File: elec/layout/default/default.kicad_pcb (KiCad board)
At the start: 4 copper layers, 76 x 144 mm, 118 parts, among them J1 ?, J2 ?, Q1 ?, Q2 ?, SW1 ?, SW10 ?, SW11 ?, SW12 ?, SW13 ?, SW14 ?, SW15 ?, SW16 ?, SW17 ?, SW18 ?, SW19 ?, SW2 ?, SW20 ?, SW21 ?, SW22 ?, SW23 ?, SW24 ?, SW25 ?, SW26 ?, SW27 ?, SW28 ?, SW29 ?, SW3 ?, SW30 ?, SW31 ?, SW32 ?, SW33 ?, SW34 ?, SW35 ?, SW36 ?, SW37 ?, SW38 ?, SW39 ?, SW4 ?, SW40 ?, SW5 ?, SW6 ?, SW7 ?, SW8 ?, SW9 ?, U1 ?, U2 ?, U3 ?, U4 ?, U5 ?, U6 ?

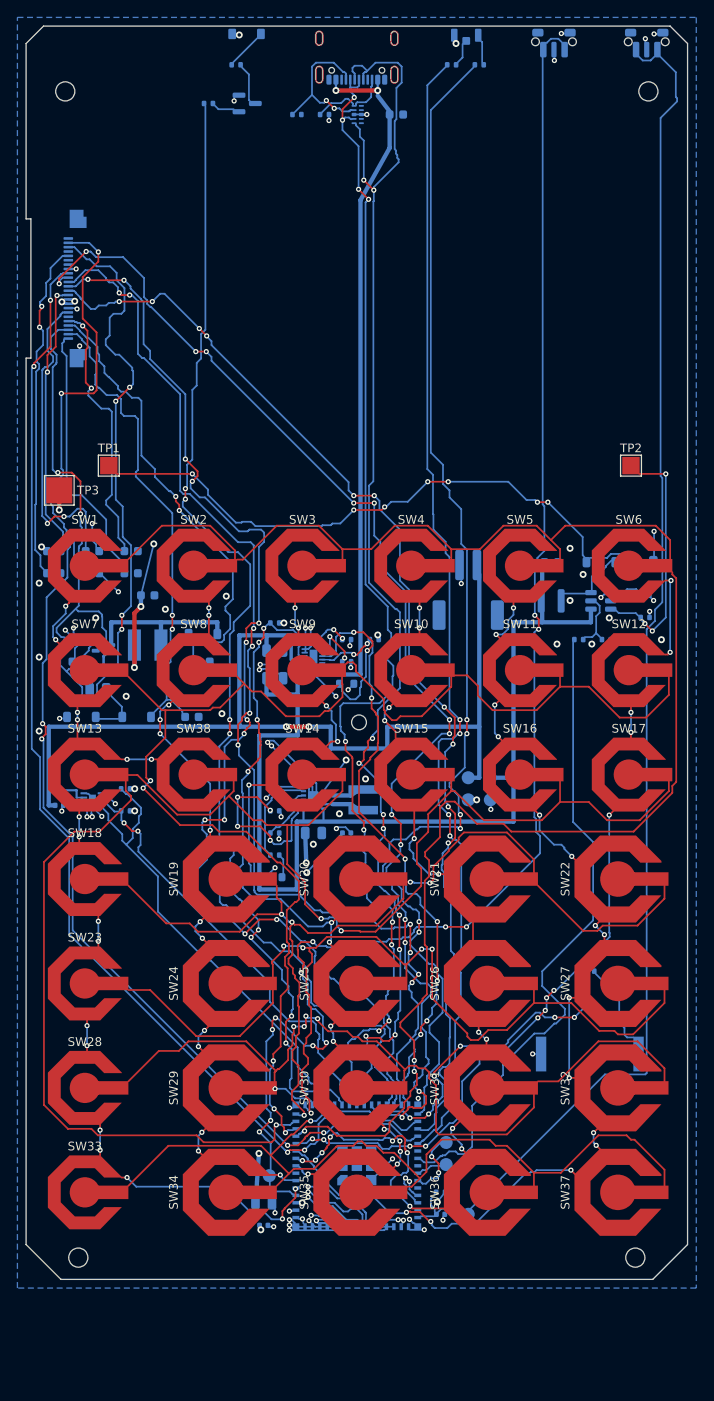
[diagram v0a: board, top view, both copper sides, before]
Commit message: mip: LS032 circuit, 155 mm board, six-LED sliver
display.ato: the e-paper booster is replaced by a TPS610997 5 V boost
(VDD and VDDA together, as Sharp allows), J2 is the Hirose FH34SRJ-10S with
panel pin n on connector pin n, and an RV-8263-C7 on the I2C bus supplies
EXTCOMIN from CLKOUT, gated by CLKOE on IO36. Footprints for the three from
the Hirose catalogue, TI YFF0006 drawing and Micro Crystal datasheet.

Board: variant.py DROP = 11, BOARD_H = 155, glass Y 12..59.02; the board
file stretched once by mip_drop_board.py, FPC notch re-centred on the new
tail, stale zone fills dropped. Placement table re-keyed for the renumbered
designators with the new display block; route_power loses the e-paper
booster's routes. Sliver is 72 mm with six LEDs.

The netlist still has to be imported in KiCad before placement and routing.

Co-Authored-By: Claude Opus 5.5 (1M context) <noreply@anthropic.com>
Claude-Session: https://claude.ai/code/session_01Fsrot3PauY1JdFC7HgzJ33
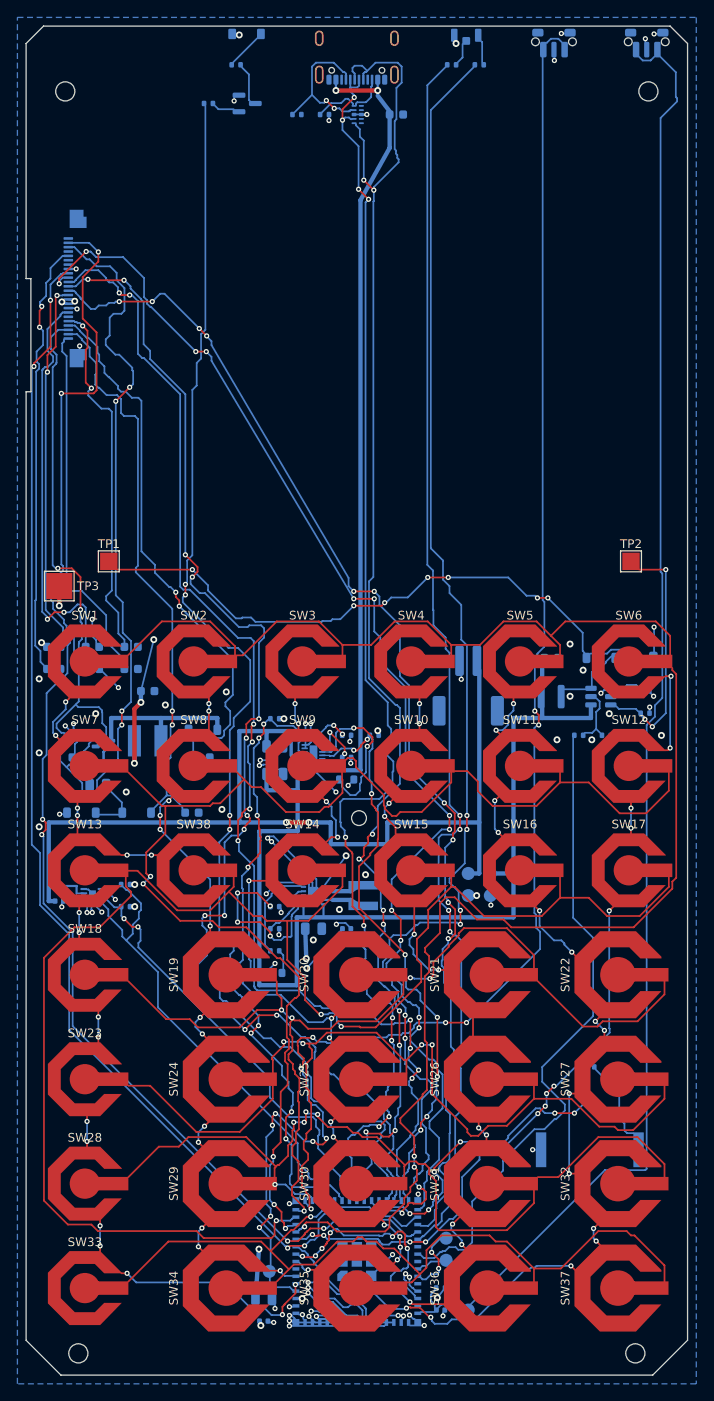
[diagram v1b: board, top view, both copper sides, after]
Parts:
- moved LS1 11.0 mm to (64.8, 129.1)
- moved BT1 11.0 mm to (50.8, 75.8)
- moved C10 11.0 mm to (3.17, 71.3)
- moved C11 11.0 mm to (7.62, 71.3)
- moved C12 11.0 mm to (12.1, 71.3)
- moved C16 11.0 mm to (14.0, 76.4)
- moved C17 11.0 mm to (20.3, 84.0)
- moved C18 11.0 mm to (8.26, 87.2)
- moved C19 11.0 mm to (19.1, 90.4)
- moved C2 11.0 mm to (28.6, 82.8)
- moved C20 11.0 mm to (71.1, 72.6)
- moved C21 11.0 mm to (60.3, 72.6)
- moved C22 11.0 mm to (71.1, 76.4)
- moved C3 11.0 mm to (28.6, 85.9)
- moved C4 11.0 mm to (33.0, 103.7)
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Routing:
- net led_red: track 148.7 -> 159.7 mm
- net epd_busy: track 133.2 -> 144.2 mm
- net epd_mosi: track 130.2 -> 141.2 mm
- net epd_dc: track 129.6 -> 140.6 mm
- net epd_cs: track 134.6 -> 145.6 mm
- net vdd: track 35.7 -> 46.7 mm
- net vcom: track 30.0 -> 41.0 mm
- net vsh1: track 30.3 -> 41.3 mm
- net vsl: track 31.9 -> 42.9 mm
- net vsh2: track 38.7 -> 49.7 mm
- net vbus: track 80.5 -> 91.5 mm
- net usb_dp: track 149.1 -> 160.1 mm
- net usb_dm: track 136.8 -> 147.8 mm
- net prevgl: track 53.7 -> 64.7 mm
- net led_green: track 131.9 -> 142.9 mm
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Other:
- board size 76 x 144 mm -> 76 x 155 mm
